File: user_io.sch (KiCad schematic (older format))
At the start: 20 parts

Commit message: Make updates per suggestions
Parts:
- removed J?: Conn_01x04, symbol Connector_Generic:Conn_01x04
- removed R? (x2): 0, symbol Device:R_Small
- removed SW?: SW_DPDT_x2, symbol Switch:SW_DPDT_x2
- removed SW?: SW_Push, symbol Switch:SW_Push
- added C11, C13: 20p, symbol Device:C_Small
- added C18, C19, C7, C9: 100n, symbol Device:C_Small
- added HSE1: 8MHz, symbol Device:Crystal_GND23_Small
- added J4: Conn_01x06_Male, symbol Connector:Conn_01x06_Male
- added J5: Conn_01x05_Male, symbol Connector:Conn_01x05_Male
- added J6, J8: Conn_01x04_Male, symbol Connector:Conn_01x04_Male
- added R12, R14, R15, R17, R18, R20, R21, R22: 10k, symbol Device:R_Small
- added R16: 390, symbol Device:R_Small
- added R19: 0, symbol Device:R_Small
- added SW1, SW2, SW3: SW_Push_Dual, symbol Switch:SW_Push_Dual
- gave numbers to parts that had none: 15
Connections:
- net labels added: OSC_IN, OSC_OUT, SPI_INT, SUBS_P_INT
- net labels removed: RA8875_3V_Out, RA8875_GND, RA8875_LITE, RA8875_VIN, RA8875_XM, RA8875_XP, RA8875_YM, RA8875_YP, SCREEN_INT, SCREEN_MISO, SCREEN_MOSI, SCREEN_NRST, SCREEN_NSS, SCREEN_SCK, SCREEN_WAIT
- wire segments 101 -> 182
- no-connect marks 47 -> 44
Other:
- note added: "External Oscillator"
- note added: "Serial Communication Header Pins\n"
- note added: "User IO to DAC SPI"
- note added: "User Pushbutton\n"
- note removed: "Known No-Connects"
- note removed: "Power/Gnd"
- note removed: "Signals"
- note removed: "USART Debug Connection"
- note removed: "User IO to DAC Subsystem Communication"
- moved on the sheet: C10, C12, C14, C15, C16, C17, C8, J3, J7, R11, R13, R23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

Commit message: Make most changes for final design
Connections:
- net +3V3: now also R22.1
- net GND: no longer R22.1
- net USART_RX: now also J8.3 (Pin_3); no longer J8.2 (Pin_2)
- net USART_TX: now also J8.2 (Pin_2); no longer J8.3 (Pin_3)
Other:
- moved on the sheet: R22
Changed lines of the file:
@@
 L power:+3.3V #PWR053
 U 1 1 6055EB95
-P 9900 4600
-F 0 "#PWR053" H 9900 4450 50  0001 C CNN
-F 1 "+3.3V" H 9915 4773 50  0000 C CNN
-F 2 "" H 9900 4600 50  0001 C CNN
-F 3 "" H 9900 4600 50  0001 C CNN
-	1    9900 4600
+P 9900 4400
+F 0 "#PWR053" H 9900 4250 50  0001 C CNN
+F 1 "+3.3V" H 9915 4573 50  0000 C CNN
+F 2 "" H 9900 4400 50  0001 C CNN
+F 3 "" H 9900 4400 50  0001 C CNN
+	1    9900 4400
 	1    0    0    -1
 $EndComp
@@
 	9900 4950 9950 4950
 Wire Wire Line
-	9900 4600 9900 4650
-Wire Wire Line
 	9900 4650 9950 4650
-Text Label 9700 4850 2    50   ~ 0
+Text Label 9600 4750 2    50   ~ 0
 USART_RX
-Text Label 9700 4750 2    50   ~ 0
+Text Label 9600 4850 2    50   ~ 0
 USART_TX
 Wire Notes Line
@@
 L Device:R_Small R22
 U 1 1 60A388CB
-P 9750 5000
-F 0 "R22" H 9880 4960 50  0000 R CNN
-F 1 "10k" H 9920 5030 50  0000 R CNN
-F 2 "" H 9750 5000 50  0001 C CNN
-F 3 "~" H 9750 5000 50  0001 C CNN
-	1    9750 5000
-	-1   0    0    1
-$EndComp
-Wire Wire Line
-	9750 5100 9900 5100
-Wire Wire Line
-	9900 5100 9900 5150
-Wire Wire Line
-	9750 4900 9750 4850
-Wire Wire Line
-	9750 4850 9950 4850
-Wire Wire Line
-	9700 4850 9750 4850
-Connection ~ 9750 4850
-Wire Wire Line
-	9900 4950 9900 5100
-Connection ~ 9900 5100
-Wire Wire Line
-	9700 4750 9950 4750
+P 9750 4600
+F 0 "R22" H 9718 4640 50  0000 R CNN
+F 1 "10k" H 9714 4570 50  0000 R CNN
+F 2 "" H 9750 4600 50  0001 C CNN
+F 3 "~" H 9750 4600 50  0001 C CNN
+	1    9750 4600
+	1    0    0    -1
+$EndComp
 Wire Notes Line
 	10350 4150 10350 5300
@@
 Text Notes 5400 700  0    50   ~ 0
 User Pushbutton\n
+Wire Wire Line
+	9900 4950 9900 5150
+Wire Wire Line
+	9600 4750 9750 4750
+Wire Wire Line
+	9600 4850 9950 4850
+Wire Wire Line
+	9750 4700 9750 4750
+Connection ~ 9750 4750
+Wire Wire Line
+	9750 4750 9950 4750
+Wire Wire Line
+	9750 4500 9750 4450
+Wire Wire Line
+	9750 4450 9900 4450
+Wire Wire Line
+	9900 4450 9900 4400
+Wire Wire Line
+	9900 4450 9900 4650
+Connection ~ 9900 4450
 $EndSCHEMATC

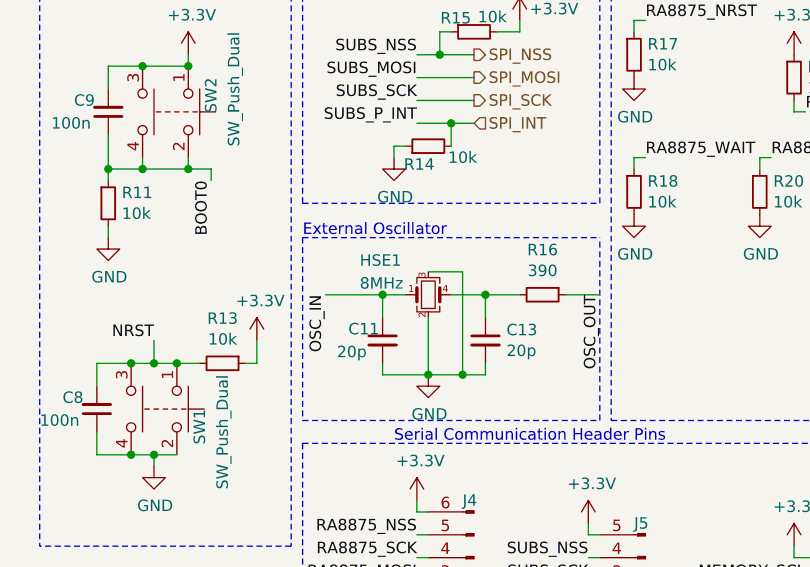
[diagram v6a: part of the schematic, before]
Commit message: Final iteration before pcb design review
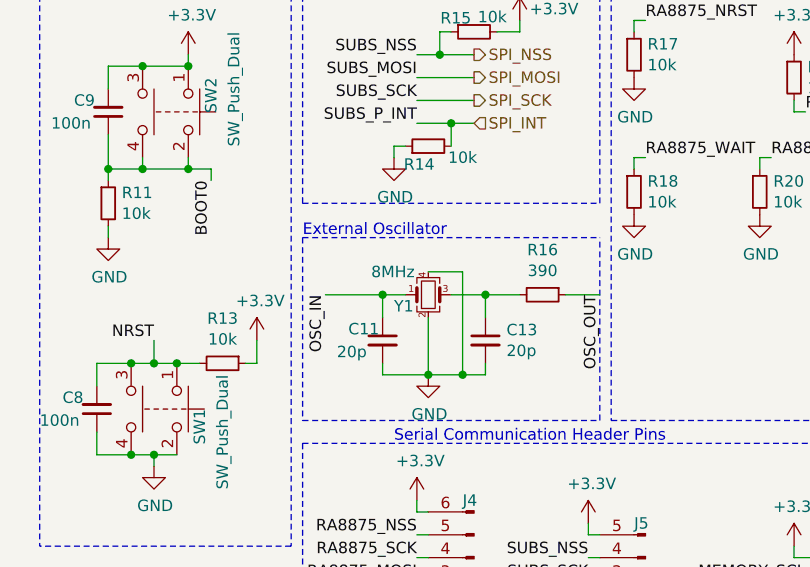
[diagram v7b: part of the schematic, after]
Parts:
- removed HSE1: 8MHz, symbol Device:Crystal_GND23_Small
- added Y1: 8MHz, Crystal:Crystal_SMD_Abracon_ABM10-4Pin_2.5x2.0mm, symbol Device:Crystal_GND24_Small
- C10, C11, C12, C13, C14, C15, C16, C17, C18, C19: footprint (none) -> Capacitor_SMD:C_0603_1608Metric
- C7, C8, C9: footprint (none) -> Capacitor_SMD:C_0805_2012Metric
- J3, J4, J5, J6: footprint (none) -> Connector_PinHeader_2.54mm:PinHeader_1x38_P2.54mm_Vertical
- J7: footprint (none) -> Connector_PinSocket_2.54mm:PinSocket_1x07_P2.54mm_Vertical
- J8: footprint (none) -> Connector_PinHeader_2.54mm:PinHeader_1x08_P2.54mm_Vertical
- R11, R12, R13, R14, R15, R16, R17, R18, R19, R20, R21, R22, R23, R24: footprint (none) -> Resistor_SMD:R_0603_1608Metric
- SW1, SW2, SW3: footprint (none) -> Button_Switch_SMD:SW_SPST_EVPBF
- U4: footprint (none) -> Package_SO:TSSOP-8_4.4x3mm_P0.65mm
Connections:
- net GND: now also Y1.2, Y1.4
- net OSC_IN: now also Y1.1
- net at C13.1, R16.2: now also Y1.3
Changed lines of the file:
@@
 F 0 "U4" H 7800 1750 50  0000 C CNN
 F 1 "CAT24C256" H 7800 1650 50  0000 C CNN
-F 2 "" H 8100 1400 50  0001 C CNN
+F 2 "Package_SO:TSSOP-8_4.4x3mm_P0.65mm" H 8100 1400 50  0001 C CNN
 F 3 "https://www.onsemi.cn/PowerSolutions/document/CAT24C256-D.PDF" H 8100 1400 50  0001 C CNN
 	1    8100 1400
@@
 F 0 "J7" H 10050 2400 50  0000 C CNN
 F 1 "Conn_01x15_Female" H 10100 4050 50  0000 C CNN
-F 2 "" H 10100 3200 50  0001 C CNN
+F 2 "Connector_PinSocket_2.54mm:PinSocket_1x07_P2.54mm_Vertical" H 10100 3200 50  0001 C CNN
 F 3 "~" H 10100 3200 50  0001 C CNN
 	1    10100 3200
@@
 F 0 "R23" H 9835 1395 50  0000 L CNN
 F 1 "R_2k2" H 9830 1310 50  0000 L CNN
-F 2 "" H 9800 1350 50  0001 C CNN
+F 2 "Resistor_SMD:R_0603_1608Metric" H 9800 1350 50  0001 C CNN
 F 3 "~" H 9800 1350 50  0001 C CNN
 	1    9800 1350
@@
 F 0 "R24" H 10180 1400 50  0000 L CNN
 F 1 "R_2k2" H 10185 1305 50  0000 L CNN
-F 2 "" H 10150 1350 50  0001 C CNN
+F 2 "Resistor_SMD:R_0603_1608Metric" H 10150 1350 50  0001 C CNN
 F 3 "~" H 10150 1350 50  0001 C CNN
 	1    10150 1350
@@
 F 0 "R11" H 5759 3146 50  0000 L CNN
 F 1 "10k" H 5759 3055 50  0000 L CNN
-F 2 "" H 5700 3100 50  0001 C CNN
+F 2 "Resistor_SMD:R_0603_1608Metric" H 5700 3100 50  0001 C CNN
 F 3 "~" H 5700 3100 50  0001 C CNN
 	1    5700 3100
@@
 F 0 "J3" H 6850 1500 50  0000 C CNN
 F 1 "Conn_02x05_Odd_Even" H 7000 900 50  0000 C CNN
-F 2 "" H 6800 1200 50  0001 C CNN
+F 2 "Connector_PinHeader_2.54mm:PinHeader_1x38_P2.54mm_Vertical" H 6800 1200 50  0001 C CNN
 F 3 "~" H 6800 1200 50  0001 C CNN
 	1    6800 1200
@@
 F 0 "C10" H 6730 5860 50  0000 L CNN
 F 1 "100n" H 6725 5740 50  0000 L CNN
-F 2 "" H 6700 5800 50  0001 C CNN
+F 2 "Capacitor_SMD:C_0603_1608Metric" H 6700 5800 50  0001 C CNN
 F 3 "~" H 6700 5800 50  0001 C CNN
 	1    6700 5800
@@
 F 0 "C12" H 7080 5860 50  0000 L CNN
 F 1 "4.7u" H 7075 5740 50  0000 L CNN
-F 2 "" H 7050 5800 50  0001 C CNN
+F 2 "Capacitor_SMD:C_0603_1608Metric" H 7050 5800 50  0001 C CNN
 F 3 "~" H 7050 5800 50  0001 C CNN
 	1    7050 5800
@@
 F 0 "C14" H 7425 5860 50  0000 L CNN
 F 1 "100n" H 7420 5745 50  0000 L CNN
-F 2 "" H 7400 5800 50  0001 C CNN
+F 2 "Capacitor_SMD:C_0603_1608Metric" H 7400 5800 50  0001 C CNN
 F 3 "~" H 7400 5800 50  0001 C CNN
 	1    7400 5800
@@
 F 0 "C16" H 8170 5865 50  0000 L CNN
 F 1 "1u" H 8180 5740 50  0000 L CNN
-F 2 "" H 8150 5800 50  0001 C CNN
+F 2 "Capacitor_SMD:C_0603_1608Metric" H 8150 5800 50  0001 C CNN
 F 3 "~" H 8150 5800 50  0001 C CNN
 	1    8150 5800
@@
 F 0 "C17" H 8490 5865 50  0000 L CNN
 F 1 "10n" H 8475 5735 50  0000 L CNN
-F 2 "" H 8450 5800 50  0001 C CNN
+F 2 "Capacitor_SMD:C_0603_1608Metric" H 8450 5800 50  0001 C CNN
 F 3 "~" H 8450 5800 50  0001 C CNN
 	1    8450 5800
@@
 F 0 "C15" H 7735 5865 50  0000 L CNN
 F 1 "100n" H 7720 5740 50  0000 L CNN
-F 2 "" H 7700 5800 50  0001 C CNN
+F 2 "Capacitor_SMD:C_0603_1608Metric" H 7700 5800 50  0001 C CNN
 F 3 "~" H 7700 5800 50  0001 C CNN
 	1    7700 5800
@@
 F 0 "R13" V 6004 3800 50  0000 C CNN
 F 1 "10k" V 6095 3800 50  0000 C CNN
-F 2 "" H 6200 3800 50  0001 C CNN
+F 2 "Resistor_SMD:R_0603_1608Metric" H 6200 3800 50  0001 C CNN
 F 3 "~" H 6200 3800 50  0001 C CNN
 	1    6200 3800
@@
 F 0 "C8" H 5800 3950 50  0000 R CNN
 F 1 "100n" H 5900 4050 50  0000 R CNN
-F 2 "" H 5650 4000 50  0001 C CNN
+F 2 "Capacitor_SMD:C_0805_2012Metric" H 5650 4000 50  0001 C CNN
 F 3 "~" H 5650 4000 50  0001 C CNN
 	1    5650 4000
@@
 F 0 "J8" H 10200 4600 50  0000 R CNN
 F 1 "Conn_01x04_Male" V 10050 5150 50  0000 R CNN
-F 2 "" H 10150 4850 50  0001 C CNN
+F 2 "Connector_PinHeader_2.54mm:PinHeader_1x08_P2.54mm_Vertical" H 10150 4850 50  0001 C CNN
 F 3 "~" H 10150 4850 50  0001 C CNN
 	1    10150 4850
@@
 F 0 "J6" H 9050 4600 50  0000 R CNN
 F 1 "Conn_01x04_Male" H 9200 5000 50  0000 R CNN
-F 2 "" H 9000 4850 50  0001 C CNN
+F 2 "Connector_PinHeader_2.54mm:PinHeader_1x38_P2.54mm_Vertical" H 9000 4850 50  0001 C CNN
 F 3 "~" H 9000 4850 50  0001 C CNN
 	1    9000 4850
@@
 F 0 "J5" H 8100 4500 50  0000 R CNN
 F 1 "Conn_01x05_Male" H 8200 5000 50  0000 R CNN
-F 2 "" H 8050 4750 50  0001 C CNN
+F 2 "Connector_PinHeader_2.54mm:PinHeader_1x38_P2.54mm_Vertical" H 8050 4750 50  0001 C CNN
 F 3 "~" H 8050 4750 50  0001 C CNN
 	1    8050 4750
@@
 F 0 "R14" V 7020 2890 50  0000 C CNN
 F 1 "10k" V 7050 2700 50  0000 C CNN
-F 2 "" H 7100 2850 50  0001 C CNN
+F 2 "Resistor_SMD:R_0603_1608Metric" H 7100 2850 50  0001 C CNN
 F 3 "~" H 7100 2850 50  0001 C CNN
 	1    7100 2850
@@
 F 0 "R18" H 8059 3096 50  0000 L CNN
 F 1 "10k" H 8059 3005 50  0000 L CNN
-F 2 "" H 8000 3050 50  0001 C CNN
+F 2 "Resistor_SMD:R_0603_1608Metric" H 8000 3050 50  0001 C CNN
 F 3 "~" H 8000 3050 50  0001 C CNN
 	1    8000 3050
@@
 F 0 "R20" H 8609 3096 50  0000 L CNN
 F 1 "10k" H 8609 3005 50  0000 L CNN
-F 2 "" H 8550 3050 50  0001 C CNN
+F 2 "Resistor_SMD:R_0603_1608Metric" H 8550 3050 50  0001 C CNN
 F 3 "~" H 8550 3050 50  0001 C CNN
 	1    8550 3050
@@
 F 0 "J4" H 7350 4400 50  0000 R CNN
 F 1 "Conn_01x06_Male" H 7550 5000 50  0000 R CNN
-F 2 "" H 7300 4750 50  0001 C CNN
+F 2 "Connector_PinHeader_2.54mm:PinHeader_1x38_P2.54mm_Vertical" H 7300 4750 50  0001 C CNN
 F 3 "~" H 7300 4750 50  0001 C CNN
 	1    7300 4750
@@
 F 0 "R21" H 8759 2596 50  0000 L CNN
 F 1 "10k" H 8759 2505 50  0000 L CNN
-F 2 "" H 8700 2550 50  0001 C CNN
+F 2 "Resistor_SMD:R_0603_1608Metric" H 8700 2550 50  0001 C CNN
 F 3 "~" H 8700 2550 50  0001 C CNN
 	1    8700 2550
@@
 F 0 "R17" H 8059 2496 50  0000 L CNN
 F 1 "10k" H 8059 2405 50  0000 L CNN
-F 2 "" H 8000 2450 50  0001 C CNN
+F 2 "Resistor_SMD:R_0603_1608Metric" H 8000 2450 50  0001 C CNN
 F 3 "~" H 8000 2450 50  0001 C CNN
 	1    8000 2450
@@
 F 0 "R15" V 7240 2430 50  0000 C CNN
 F 1 "10k" V 7235 2270 50  0000 C CNN
-F 2 "" H 7300 2350 50  0001 C CNN
+F 2 "Resistor_SMD:R_0603_1608Metric" H 7300 2350 50  0001 C CNN
 F 3 "~" H 7300 2350 50  0001 C CNN
 	1    7300 2350
@@
 	1400 3500 1450 3500
 $Comp
-L Device:Crystal_GND23_Small HSE?
-U 1 1 60995C2D
-P 7100 3500
-AR Path="/60454D6D/60995C2D" Ref="HSE?"  Part="1"
-AR Path="/6045302E/60995C2D" Ref="HSE1"  Part="1"
-F 0 "HSE1" H 6800 3650 50  0000 L CNN
-F 1 "8MHz" H 6800 3550 50  0000 L CNN
-F 2 "" H 7100 3500 50  0001 C CNN
-F 3 "~" H 7100 3500 50  0001 C CNN
-	1    7100 3500
-	1    0    0    -1
-$EndComp
-$Comp
 L Device:C_Small C?
 U 1 1 60995C33
@@
 F 0 "C13" H 7442 3746 50  0000 L CNN
 F 1 "20p" H 7442 3655 50  0000 L CNN
-F 2 "" H 7350 3700 50  0001 C CNN
+F 2 "Capacitor_SMD:C_0603_1608Metric" H 7350 3700 50  0001 C CNN
 F 3 "~" H 7350 3700 50  0001 C CNN
 	1    7350 3700
@@
 F 0 "C11" H 6750 3750 50  0000 L CNN
 F 1 "20p" H 6700 3650 50  0000 L CNN
-F 2 "" H 6900 3700 50  0001 C CNN
+F 2 "Capacitor_SMD:C_0603_1608Metric" H 6900 3700 50  0001 C CNN
 F 3 "~" H 6900 3700 50  0001 C CNN
 	1    6900 3700
@@
 F 0 "R16" V 7404 3500 50  0000 C CNN
 F 1 "390" V 7495 3500 50  0000 C CNN
-F 2 "" H 7600 3500 50  0001 C CNN
+F 2 "Resistor_SMD:R_0603_1608Metric" H 7600 3500 50  0001 C CNN
 F 3 "~" H 7600 3500 50  0001 C CNN
 	1    7600 3500
@@
 F 0 "R22" H 9718 4640 50  0000 R CNN
 F 1 "10k" H 9714 4570 50  0000 R CNN
-F 2 "" H 9750 4600 50  0001 C CNN
+F 2 "Resistor_SMD:R_0603_1608Metric" H 9750 4600 50  0001 C CNN
 F 3 "~" H 9750 4600 50  0001 C CNN
 	1    9750 4600
@@
 F 0 "SW2" H 5900 2800 50  0000 L CNN
 F 1 "SW_Push_Dual" H 5700 2900 50  0000 L CNN
-F 2 "" H 6050 2900 50  0001 C CNN
+F 2 "Button_Switch_SMD:SW_SPST_EVPBF" H 6050 2900 50  0001 C CNN
 F 3 "~" H 6050 2900 50  0001 C CNN
 	1    6050 2700
@@
 F 0 "C9" H 5850 2650 50  0000 R CNN
 F 1 "100n" H 5950 2750 50  0000 R CNN
-F 2 "" H 5700 2700 50  0001 C CNN
+F 2 "Capacitor_SMD:C_0805_2012Metric" H 5700 2700 50  0001 C CNN
 F 3 "~" H 5700 2700 50  0001 C CNN
 	1    5700 2700
@@
 F 0 "SW1" H 6000 4100 50  0000 L CNN
 F 1 "SW_Push_Dual" H 5850 4200 50  0000 L CNN
-F 2 "" H 6000 4200 50  0001 C CNN
+F 2 "Button_Switch_SMD:SW_SPST_EVPBF" H 6000 4200 50  0001 C CNN
 F 3 "~" H 6000 4200 50  0001 C CNN
 	1    6000 4000
@@
 F 0 "R19" H 8609 1696 50  0000 L CNN
 F 1 "0" H 8609 1605 50  0000 L CNN
-F 2 "" H 8550 1650 50  0001 C CNN
+F 2 "Resistor_SMD:R_0603_1608Metric" H 8550 1650 50  0001 C CNN
 F 3 "~" H 8550 1650 50  0001 C CNN
 	1    8550 1650
@@
 F 0 "C18" H 9035 1510 50  0000 L CNN
 F 1 "100n" H 9000 1400 50  0000 L CNN
-F 2 "" H 9200 1450 50  0001 C CNN
+F 2 "Capacitor_SMD:C_0603_1608Metric" H 9200 1450 50  0001 C CNN
 F 3 "~" H 9200 1450 50  0001 C CNN
 	1    9200 1450
@@
 F 0 "C19" H 9505 1510 50  0000 L CNN
 F 1 "100n" H 9505 1390 50  0000 L CNN
-F 2 "" H 9500 1450 50  0001 C CNN
+F 2 "Capacitor_SMD:C_0603_1608Metric" H 9500 1450 50  0001 C CNN
 F 3 "~" H 9500 1450 50  0001 C CNN
 	1    9500 1450
@@
 F 0 "SW3" H 6100 1300 50  0000 L CNN
 F 1 "SW_Push_Dual" H 5800 1400 50  0000 L CNN
-F 2 "" H 6100 1400 50  0001 C CNN
+F 2 "Button_Switch_SMD:SW_SPST_EVPBF" H 6100 1400 50  0001 C CNN
 F 3 "~" H 6100 1400 50  0001 C CNN
 	1    6100 1200
@@
 F 0 "C7" H 5800 1200 50  0000 R CNN
 F 1 "100n" H 5870 1305 50  0000 R CNN
-F 2 "" H 5650 1250 50  0001 C CNN
+F 2 "Capacitor_SMD:C_0805_2012Metric" H 5650 1250 50  0001 C CNN
 F 3 "~" H 5650 1250 50  0001 C CNN
 	1    5650 1250
@@
 F 0 "R12" H 5959 1596 50  0000 L CNN
 F 1 "10k" H 5959 1505 50  0000 L CNN
-F 2 "" H 5900 1550 50  0001 C CNN
+F 2 "Resistor_SMD:R_0603_1608Metric" H 5900 1550 50  0001 C CNN
 F 3 "~" H 5900 1550 50  0001 C CNN
 	1    5900 1550
@@
 	9900 4450 9900 4650
 Connection ~ 9900 4450
+$Comp
+L Device:Crystal_GND24_Small Y1
+U 1 1 60731763
+P 7100 3500
+F 0 "Y1" H 6950 3450 50  0000 L CNN
+F 1 "8MHz" H 6850 3600 50  0000 L CNN
+F 2 "Crystal:Crystal_SMD_Abracon_ABM10-4Pin_2.5x2.0mm" H 7100 3500 50  0001 C CNN
+F 3 "~" H 7100 3500 50  0001 C CNN
+	1    7100 3500
+	1    0    0    -1
+$EndComp
 $EndSCHEMATC

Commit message: Finish schematic
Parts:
- C10, C11, C12, C13, C14, C15, C16, C18, C19, C7, C8, C9: Min Voltage Rating (none) -> 3.3 V
- J3: Description (none) -> STLink header for programming/debugging
- J4: Description (none) -> Header for Screen SPI Debug
- J5: Description (none) -> Header for subsystem SPI Debug
- J6: Description (none) -> Header for EEPROM I2C Debug
- J7: Description (none) -> Header for RA8875 pins
- J8: Description (none) -> Header for F0 UART Debug
- SW1, SW2: Description (none) -> Pushbuttons for NRST/BOOT
- SW3: Description (none) -> User push button
- U3: Description (none) -> F0 processor for User IO
- U4: Description (none) -> EEPROM for storage
- Y1: Description (none) -> HSE crystals
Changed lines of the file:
@@
 F 2 "Package_QFP:LQFP-64_10x10mm_P0.5mm" H 1550 2500 50  0001 R CNN
 F 3 "http://www.st.com/st-web-ui/static/active/en/resource/technical/document/datasheet/DM00039193.pdf" H 2050 4200 50  0001 C CNN
+F 4 "F0 processor for User IO" H 2050 4200 50  0001 C CNN "Description"
 	1    2050 4200
 	1    0    0    -1
@@
 F 2 "Package_SO:TSSOP-8_4.4x3mm_P0.65mm" H 8100 1400 50  0001 C CNN
 F 3 "https://www.onsemi.cn/PowerSolutions/document/CAT24C256-D.PDF" H 8100 1400 50  0001 C CNN
+F 4 "EEPROM for storage" H 8100 1400 50  0001 C CNN "Description"
 	1    8100 1400
 	1    0    0    -1
@@
 F 2 "Connector_PinSocket_2.54mm:PinSocket_1x07_P2.54mm_Vertical" H 10100 3200 50  0001 C CNN
 F 3 "~" H 10100 3200 50  0001 C CNN
+F 4 "Header for RA8875 pins" H 10100 3200 50  0001 C CNN "Description"
 	1    10100 3200
 	1    0    0    -1
@@
 F 2 "Connector_PinHeader_2.54mm:PinHeader_1x38_P2.54mm_Vertical" H 6800 1200 50  0001 C CNN
 F 3 "~" H 6800 1200 50  0001 C CNN
+F 4 "STLink header for programming/debugging" H 6800 1200 50  0001 C CNN "Description"
 	1    6800 1200
 	1    0    0    -1
@@
 F 2 "Capacitor_SMD:C_0603_1608Metric" H 6700 5800 50  0001 C CNN
 F 3 "~" H 6700 5800 50  0001 C CNN
+F 4 "3.3 V" H 6700 5800 50  0001 C CNN "Min Voltage Rating"
 	1    6700 5800
 	1    0    0    -1
@@
 F 2 "Capacitor_SMD:C_0603_1608Metric" H 7050 5800 50  0001 C CNN
 F 3 "~" H 7050 5800 50  0001 C CNN
+F 4 "3.3 V" H 7050 5800 50  0001 C CNN "Min Voltage Rating"
 	1    7050 5800
 	1    0    0    -1
@@
 F 2 "Capacitor_SMD:C_0603_1608Metric" H 7400 5800 50  0001 C CNN
 F 3 "~" H 7400 5800 50  0001 C CNN
+F 4 "3.3 V" H 7400 5800 50  0001 C CNN "Min Voltage Rating"
 	1    7400 5800
 	1    0    0    -1
@@
 F 2 "Capacitor_SMD:C_0603_1608Metric" H 8150 5800 50  0001 C CNN
 F 3 "~" H 8150 5800 50  0001 C CNN
+F 4 "3.3 V" H 8150 5800 50  0001 C CNN "Min Voltage Rating"
 	1    8150 5800
 	1    0    0    -1
@@
 F 2 "Capacitor_SMD:C_0603_1608Metric" H 7700 5800 50  0001 C CNN
 F 3 "~" H 7700 5800 50  0001 C CNN
+F 4 "3.3 V" H 7700 5800 50  0001 C CNN "Min Voltage Rating"
 	1    7700 5800
 	1    0    0    -1
@@
 F 2 "Capacitor_SMD:C_0805_2012Metric" H 5650 4000 50  0001 C CNN
 F 3 "~" H 5650 4000 50  0001 C CNN
+F 4 "3.3 V" H 5650 4000 50  0001 C CNN "Min Voltage Rating"
 	1    5650 4000
 	-1   0    0    1
@@
 F 2 "Connector_PinHeader_2.54mm:PinHeader_1x08_P2.54mm_Vertical" H 10150 4850 50  0001 C CNN
 F 3 "~" H 10150 4850 50  0001 C CNN
+F 4 "Header for F0 UART Debug" H 10150 4850 50  0001 C CNN "Description"
 	1    10150 4850
 	-1   0    0    1
@@
 F 2 "Connector_PinHeader_2.54mm:PinHeader_1x38_P2.54mm_Vertical" H 9000 4850 50  0001 C CNN
 F 3 "~" H 9000 4850 50  0001 C CNN
+F 4 "Header for EEPROM I2C Debug" H 9000 4850 50  0001 C CNN "Description"
 	1    9000 4850
 	-1   0    0    1
@@
 F 2 "Connector_PinHeader_2.54mm:PinHeader_1x38_P2.54mm_Vertical" H 8050 4750 50  0001 C CNN
 F 3 "~" H 8050 4750 50  0001 C CNN
+F 4 "Header for subsystem SPI Debug" H 8050 4750 50  0001 C CNN "Description"
 	1    8050 4750
 	-1   0    0    1
@@
 F 2 "Connector_PinHeader_2.54mm:PinHeader_1x38_P2.54mm_Vertical" H 7300 4750 50  0001 C CNN
 F 3 "~" H 7300 4750 50  0001 C CNN
+F 4 "Header for Screen SPI Debug" H 7300 4750 50  0001 C CNN "Description"
 	1    7300 4750
 	-1   0    0    1
@@
 F 2 "Capacitor_SMD:C_0603_1608Metric" H 7350 3700 50  0001 C CNN
 F 3 "~" H 7350 3700 50  0001 C CNN
+F 4 "3.3 V" H 7350 3700 50  0001 C CNN "Min Voltage Rating"
 	1    7350 3700
 	1    0    0    -1
@@
 F 2 "Capacitor_SMD:C_0603_1608Metric" H 6900 3700 50  0001 C CNN
 F 3 "~" H 6900 3700 50  0001 C CNN
+F 4 "3.3 V" H 6900 3700 50  0001 C CNN "Min Voltage Rating"
 	1    6900 3700
 	1    0    0    -1
@@
 F 2 "Button_Switch_SMD:SW_SPST_EVPBF" H 6050 2900 50  0001 C CNN
 F 3 "~" H 6050 2900 50  0001 C CNN
+F 4 "Pushbuttons for NRST/BOOT" H 6050 2700 50  0001 C CNN "Description"
 	1    6050 2700
 	0    1    1    0
@@
 F 2 "Capacitor_SMD:C_0805_2012Metric" H 5700 2700 50  0001 C CNN
 F 3 "~" H 5700 2700 50  0001 C CNN
+F 4 "3.3 V" H 5700 2700 50  0001 C CNN "Min Voltage Rating"
 	1    5700 2700
 	-1   0    0    1
@@
 F 2 "Button_Switch_SMD:SW_SPST_EVPBF" H 6000 4200 50  0001 C CNN
 F 3 "~" H 6000 4200 50  0001 C CNN
+F 4 "Pushbuttons for NRST/BOOT" H 6000 4000 50  0001 C CNN "Description"
 	1    6000 4000
 	0    1    1    0
@@
 F 2 "Capacitor_SMD:C_0603_1608Metric" H 9200 1450 50  0001 C CNN
 F 3 "~" H 9200 1450 50  0001 C CNN
+F 4 "3.3 V" H 9200 1450 50  0001 C CNN "Min Voltage Rating"
 	1    9200 1450
 	1    0    0    -1
@@
 F 2 "Capacitor_SMD:C_0603_1608Metric" H 9500 1450 50  0001 C CNN
 F 3 "~" H 9500 1450 50  0001 C CNN
+F 4 "3.3 V" H 9500 1450 50  0001 C CNN "Min Voltage Rating"
 	1    9500 1450
 	1    0    0    -1
@@
 F 2 "Button_Switch_SMD:SW_SPST_EVPBF" H 6100 1400 50  0001 C CNN
 F 3 "~" H 6100 1400 50  0001 C CNN
+F 4 "User push button" H 6100 1200 50  0001 C CNN "Description"
 	1    6100 1200
 	0    1    1    0
@@
 F 2 "Capacitor_SMD:C_0805_2012Metric" H 5650 1250 50  0001 C CNN
 F 3 "~" H 5650 1250 50  0001 C CNN
+F 4 "3.3 V" H 5650 1250 50  0001 C CNN "Min Voltage Rating"
 	1    5650 1250
 	-1   0    0    1
@@
 F 2 "Crystal:Crystal_SMD_Abracon_ABM10-4Pin_2.5x2.0mm" H 7100 3500 50  0001 C CNN
 F 3 "~" H 7100 3500 50  0001 C CNN
+F 4 "HSE crystals" H 7100 3500 50  0001 C CNN "Description"
 	1    7100 3500
 	1    0    0    -1
